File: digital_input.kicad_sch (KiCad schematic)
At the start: 48 parts, among them J4 5 Pin 3.5mm, J5 5 Pin 3.5mm, U8 ULN2803A

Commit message: routed version
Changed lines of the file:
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@@
   (symbol (lib_id "Connector_Generic:Conn_01x05") (at 29.21 111.76 0) (mirror y) (unit 1)
     (in_bom yes) (on_board yes) (dnp no) (fields_autoplaced)
-    (property "Reference" "J4" (at 29.21 100.33 0)
-      (effects (font (size 1.27 1.27)))
-    )
-    (property "Value" "5 Pin 3.5mm" (at 29.21 102.87 0)
+    (property "Reference" "J4" (at 29.21 101.6 0)
+      (effects (font (size 1.27 1.27)))
+    )
+    (property "Value" "5 Pin 3.5mm" (at 29.21 104.14 0)
       (effects (font (size 1.27 1.27)))
     )
@@
   (symbol (lib_id "Connector_Generic:Conn_01x05") (at 29.21 129.54 0) (mirror y) (unit 1)
     (in_bom yes) (on_board yes) (dnp no) (fields_autoplaced)
-    (property "Reference" "J5" (at 29.21 118.11 0)
-      (effects (font (size 1.27 1.27)))
-    )
-    (property "Value" "5 Pin 3.5mm" (at 29.21 120.65 0)
-      (effects (font (size 1.27 1.27)))
-    )
+    (property "Reference" "J5" (at 29.21 119.38 0)
+      (effects (font (size 1.27 1.27)))
+    )
+    (property "Value" "5 Pin 3.5mm" (at 29.21 121.92 0)
+      (effects (font (size 1.27 1.27)))
+    )

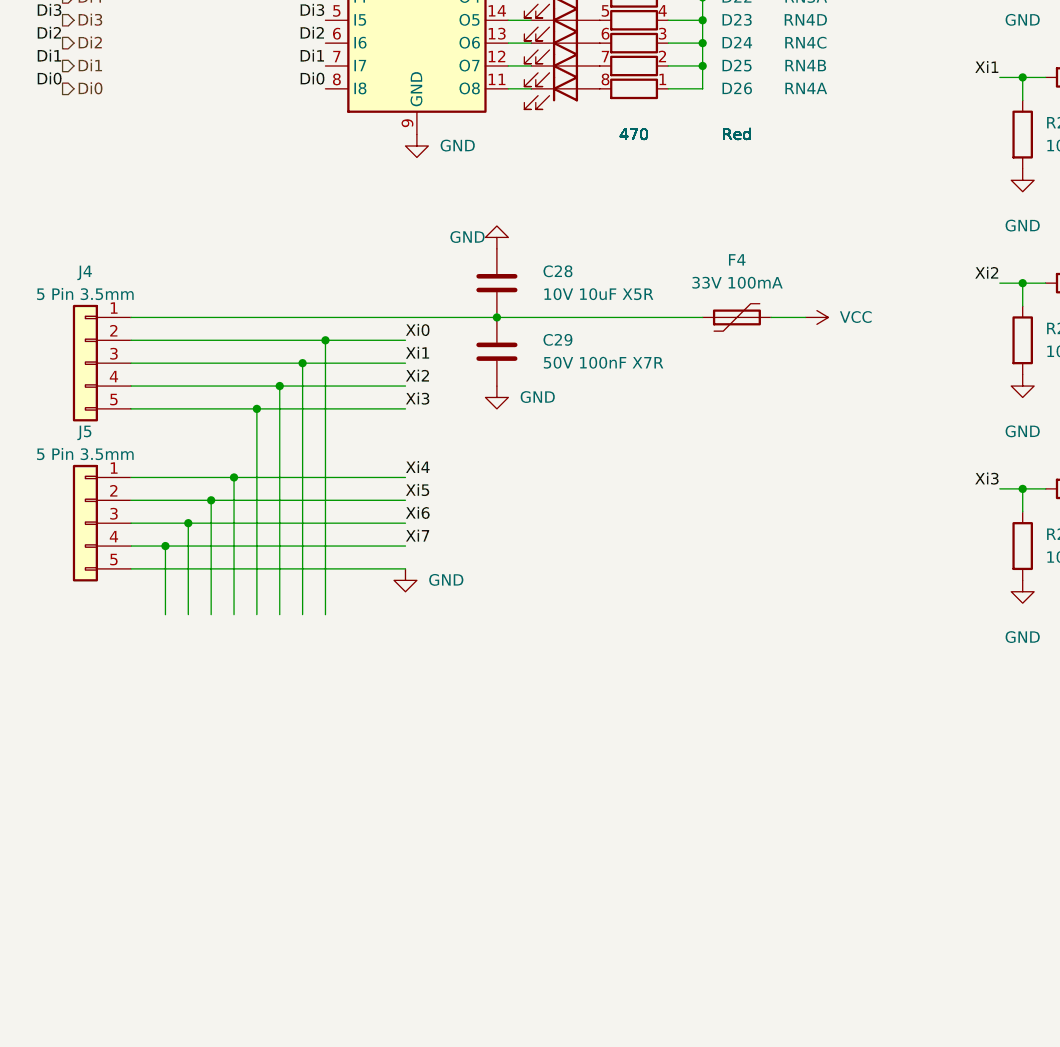
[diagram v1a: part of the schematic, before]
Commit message: Preparation for future use.
Reworked to use i2c bus expanders.
added sketch for add-on boards.
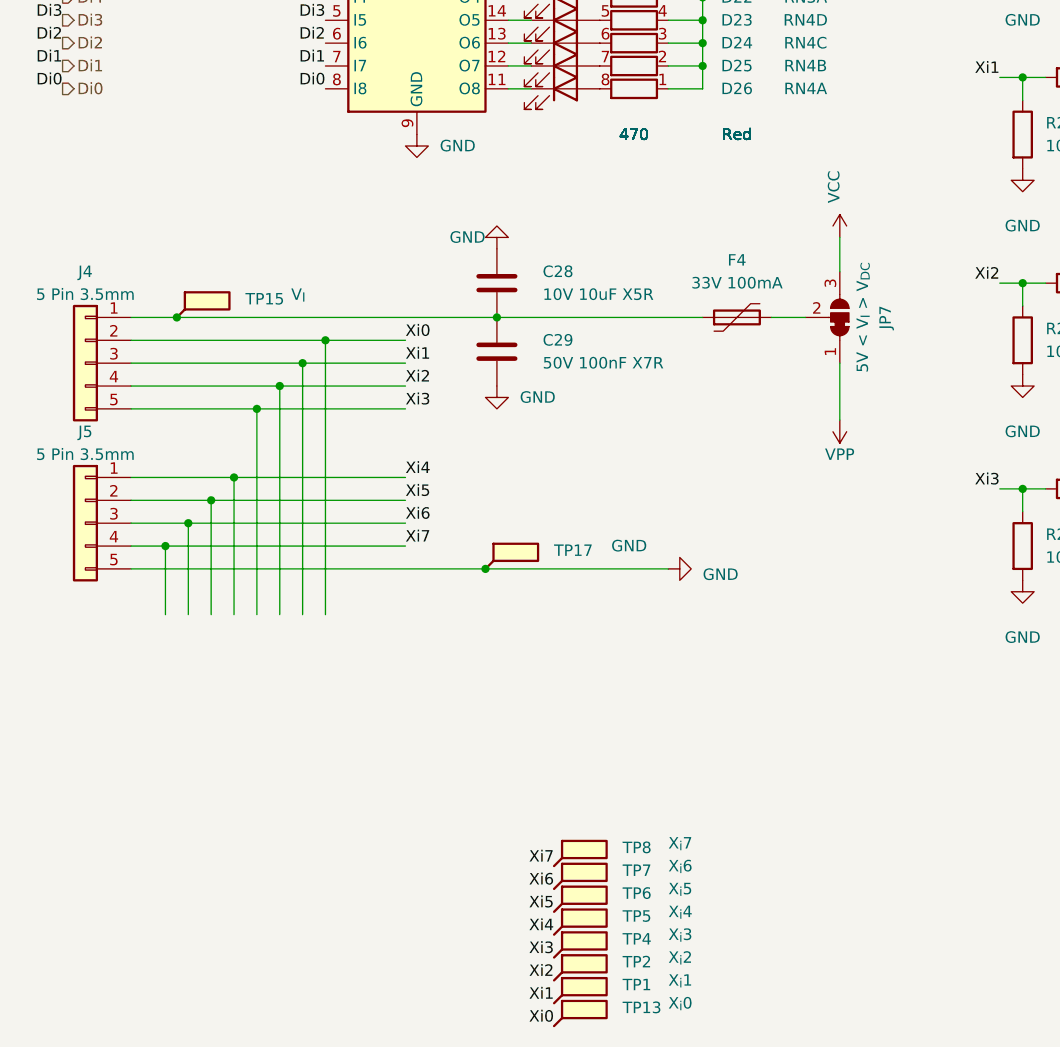
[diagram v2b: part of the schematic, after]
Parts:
- added JP7: 5V < V_{I} > V_{DC}, Connector_PinHeader_2.54mm:PinHeader_1x03_P2.54mm_Vertical, symbol Jumper:SolderJumper_3_Bridged12
- added TP1: X_{i}1, TestPoint:TestPoint_Pad_1.0x1.0mm, symbol Connector:TestPoint_Flag
- added TP13: X_{i}0, TestPoint:TestPoint_Pad_1.0x1.0mm, symbol Connector:TestPoint_Flag
- added TP15: V_{I}, TestPoint:TestPoint_Pad_1.0x1.0mm, symbol Connector:TestPoint_Flag
- added TP17: GND, TestPoint:TestPoint_Pad_1.0x1.0mm, symbol Connector:TestPoint_Flag
- added TP2: X_{i}2, TestPoint:TestPoint_Pad_1.0x1.0mm, symbol Connector:TestPoint_Flag
- added TP4: X_{i}3, TestPoint:TestPoint_Pad_1.0x1.0mm, symbol Connector:TestPoint_Flag
- added TP5: X_{i}4, TestPoint:TestPoint_Pad_1.0x1.0mm, symbol Connector:TestPoint_Flag
- added TP6: X_{i}5, TestPoint:TestPoint_Pad_1.0x1.0mm, symbol Connector:TestPoint_Flag
- added TP7: X_{i}6, TestPoint:TestPoint_Pad_1.0x1.0mm, symbol Connector:TestPoint_Flag
- added TP8: X_{i}7, TestPoint:TestPoint_Pad_1.0x1.0mm, symbol Connector:TestPoint_Flag
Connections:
- net GND: now also TP17.1
- net VCC: now also JP7.3 (B); no longer F4.2
- net Xi0: now also TP13.1
- net Xi1: now also TP1.1
- net Xi2: now also TP2.1
- net Xi3: now also TP4.1
- net Xi4: now also TP5.1
- net Xi5: now also TP6.1
- net Xi6: now also TP7.1
- net Xi7: now also TP8.1
- net at C28.2, C29.1, F4.1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: now also TP15.1
- new net: F4.2, JP7.2 (C)
- new net VPP: JP7.1 (A)
